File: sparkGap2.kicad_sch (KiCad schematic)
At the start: 44 parts, among them J1 9V, J2 IN, J3 OUT, Q1 BS170, SW2 pp, U1 TL072

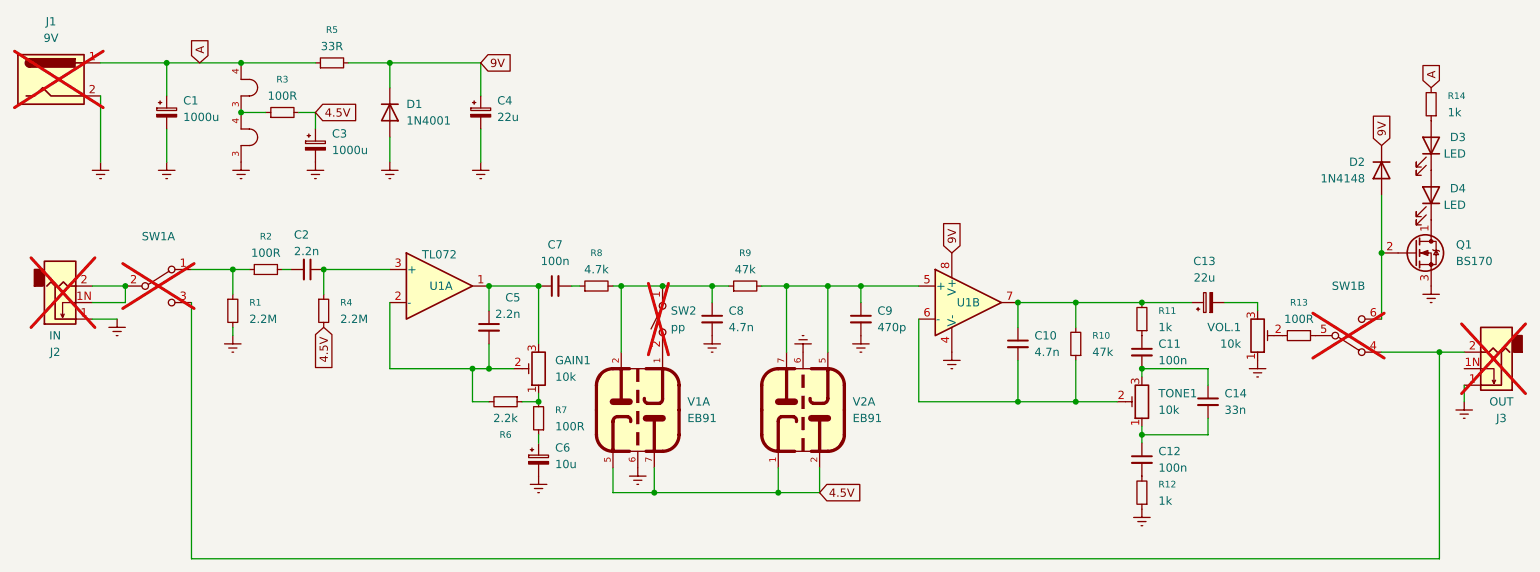
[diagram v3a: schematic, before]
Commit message: Slight adjustments to layout. Clean up component numbering.
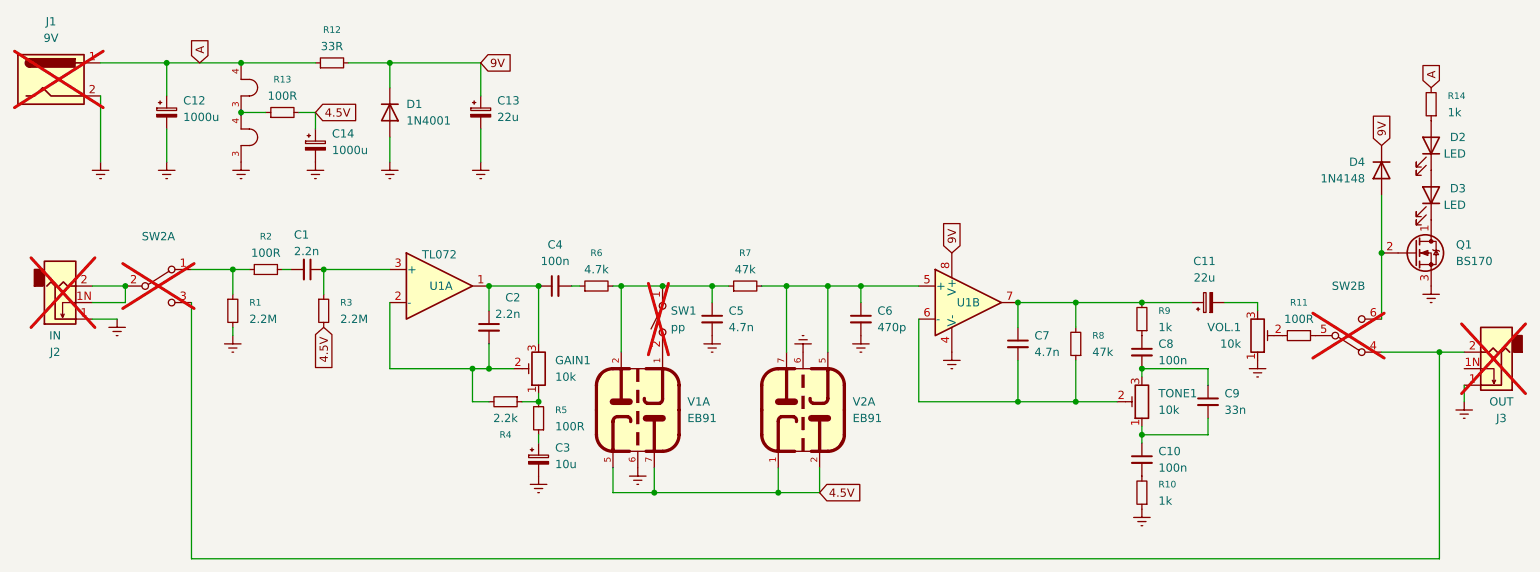
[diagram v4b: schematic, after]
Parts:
- renumbered C2 to C1, C12 to C10, C13 to C11, C1 to C12, C4 to C13, C3 to C14, C5 to C2, C6 to C3, C7 to C4, C8 to C5, C9 to C6, C10 to C7, C11 to C8, C14 to C9, D3 to D2, D4 to D3, D2 to D4, R12 to R10, R13 to R11, R5 to R12, R3 to R13, R4 to R3, R6 to R4, R7 to R5, R8 to R6, R9 to R7, R10 to R8, R11 to R9, SW2 to SW1, SW1 to SW2
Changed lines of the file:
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@@
 		(dnp no)
 		(fields_autoplaced yes)
-		(property "Reference" "R5"
+		(property "Reference" "R12"
 			(at 81.28 64.77 90)
 			(effects
@@
 			(project "sparkGap2"
 				(path "/bd6cf20e-4683-4745-aaa3-17469f6777ac"
-					(reference "R5")
+					(reference "R12")
 					(unit 1)
 				)
@@
 		(on_board yes)
 		(dnp no)
-		(property "Reference" "R6"
+		(property "Reference" "R4"
 			(at 107.95 127 90)
 			(effects
@@
 			(project "sparkGap2"
 				(path "/bd6cf20e-4683-4745-aaa3-17469f6777ac"
-					(reference "R6")
+					(reference "R4")
 					(unit 1)
 				)
@@
 		(on_board yes)
 		(dnp no)
-		(property "Reference" "C2"
+		(property "Reference" "C1"
 			(at 75.438 96.266 90)
 			(effects
@@
 			(project "sparkGap2"
 				(path "/bd6cf20e-4683-4745-aaa3-17469f6777ac"
-					(reference "C2")
+					(reference "C1")
 					(unit 1)
 				)
@@
 		(dnp no)
 		(fields_autoplaced yes)
-		(property "Reference" "C7"
+		(property "Reference" "C4"
 			(at 115.5763 97.79 90)
 			(effects
@@
 			(project "sparkGap2"
 				(path "/bd6cf20e-4683-4745-aaa3-17469f6777ac"
-					(reference "C7")
+					(reference "C4")
 					(unit 1)
 				)
@@
 		(dnp no)
 		(fields_autoplaced yes)
-		(property "Reference" "R4"
+		(property "Reference" "R3"
 			(at 82.55 106.6799 0)
 			(effects
@@
 			(project "sparkGap2"
 				(path "/bd6cf20e-4683-4745-aaa3-17469f6777ac"
-					(reference "R4")
+					(reference "R3")
 					(unit 1)
 				)
@@
 		(on_board yes)
 		(dnp no)
-		(property "Reference" "C5"
+		(property "Reference" "C2"
 			(at 110.236 105.918 0)
 			(effects
@@
 			(project "sparkGap2"
 				(path "/bd6cf20e-4683-4745-aaa3-17469f6777ac"
-					(reference "C5")
+					(reference "C2")
 					(unit 1)
 				)
@@
 		(dnp yes)
 		(fields_autoplaced yes)
-		(property "Reference" "SW1"
+		(property "Reference" "SW2"
 			(at 54.61 96.52 0)
 			(effects
@@
 			(project ""
 				(path "/bd6cf20e-4683-4745-aaa3-17469f6777ac"
-					(reference "SW1")
+					(reference "SW2")
 					(unit 1)
 				)
@@
 		(dnp no)
 		(fields_autoplaced yes)
-		(property "Reference" "C10"
+		(property "Reference" "C7"
 			(at 189.23 111.7662 0)
 			(effects
@@
 			(project "sparkGap2"
 				(path "/bd6cf20e-4683-4745-aaa3-17469f6777ac"
-					(reference "C10")
+					(reference "C7")
 					(unit 1)
 				)
@@
 		(dnp no)
 		(fields_autoplaced yes)
-		(property "Reference" "C12"
+		(property "Reference" "C10"
 			(at 208.28 129.5462 0)
 			(effects
@@
 			(project "sparkGap2"
 				(path "/bd6cf20e-4683-4745-aaa3-17469f6777ac"
-					(reference "C12")
+					(reference "C10")
 					(unit 1)
 				)
@@
 		(on_board yes)
 		(dnp no)
-		(property "Reference" "D3"
+		(property "Reference" "D2"
 			(at 255.524 81.28 90)
 			(effects
@@
 			(project "sparkGap2"
 				(path "/bd6cf20e-4683-4745-aaa3-17469f6777ac"
-					(reference "D3")
+					(reference "D2")
 					(unit 1)
 				)
@@
 		(dnp no)
 		(fields_autoplaced yes)
-		(property "Reference" "C11"
+		(property "Reference" "C8"
 			(at 208.28 113.0362 0)
 			(effects
@@
 			(project "sparkGap2"
 				(path "/bd6cf20e-4683-4745-aaa3-17469f6777ac"
-					(reference "C11")
+					(reference "C8")
 					(unit 1)
 				)
@@
 		(on_board yes)
 		(dnp no)
-		(property "Reference" "C4"
+		(property "Reference" "C13"
 			(at 106.68 75.6538 0)
 			(effects
@@
 			(project "sparkGap2"
 				(path "/bd6cf20e-4683-4745-aaa3-17469f6777ac"
-					(reference "C4")
+					(reference "C13")
 					(unit 1)
 				)
@@
 		(dnp no)
 		(fields_autoplaced yes)
-		(property "Reference" "C3"
+		(property "Reference" "C14"
 			(at 81.28 80.7338 0)
 			(effects
@@
 			(project "sparkGap2"
 				(path "/bd6cf20e-4683-4745-aaa3-17469f6777ac"
-					(reference "C3")
+					(reference "C14")
 					(unit 1)
 				)
@@
 		(dnp no)
 		(fields_autoplaced yes)
-		(property "Reference" "R10"
+		(property "Reference" "R8"
 			(at 198.12 111.7599 0)
 			(effects
@@
 			(project "sparkGap2"
 				(path "/bd6cf20e-4683-4745-aaa3-17469f6777ac"
-					(reference "R10")
+					(reference "R8")
 					(unit 1)
 				)
@@
 		(dnp yes)
 		(fields_autoplaced yes)
-		(property "Reference" "SW1"
+		(property "Reference" "SW2"
 			(at 237.49 104.14 0)
 			(effects
@@
 			(project ""
 				(path "/bd6cf20e-4683-4745-aaa3-17469f6777ac"
-					(reference "SW1")
+					(reference "SW2")
 					(unit 2)
 				)
@@
 		(on_board yes)
 		(dnp no)
-		(property "Reference" "D2"
+		(property "Reference" "D4"
 			(at 240.03 85.0899 90)
 			(effects
@@
 			(project "sparkGap2"
 				(path "/bd6cf20e-4683-4745-aaa3-17469f6777ac"
-					(reference "D2")
+					(reference "D4")
 					(unit 1)
 				)
@@
 		(dnp no)
 		(fields_autoplaced yes)
-		(property "Reference" "R12"
+		(property "Reference" "R10"
 			(at 208.28 134.6199 0)
 			(effects
@@
 			(project "sparkGap2"
 				(path "/bd6cf20e-4683-4745-aaa3-17469f6777ac"
-					(reference "R12")
+					(reference "R10")
 					(unit 1)
 				)
@@
 		(on_board yes)
 		(dnp no)
-		(property "Reference" "R9"
+		(property "Reference" "R7"
 			(at 144.78 99.06 90)
 			(effects
@@
 			(project "sparkGap2"
 				(path "/bd6cf20e-4683-4745-aaa3-17469f6777ac"
-					(reference "R9")
+					(reference "R7")
 					(unit 1)
 				)
@@
 		(dnp no)
 		(fields_autoplaced yes)
-		(property "Reference" "R7"
+		(property "Reference" "R5"
 			(at 115.57 123.1899 0)
 			(effects
@@
 			(project "sparkGap2"
 				(path "/bd6cf20e-4683-4745-aaa3-17469f6777ac"
-					(reference "R7")
+					(reference "R5")
 					(unit 1)
 				)
@@
 		(dnp no)
 		(fields_autoplaced yes)
-		(property "Reference" "C1"
+		(property "Reference" "C12"
 			(at 58.42 75.6538 0)
 			(effects
@@
 			(project "sparkGap2"
 				(path "/bd6cf20e-4683-4745-aaa3-17469f6777ac"
-					(reference "C1")
+					(reference "C12")
 					(unit 1)
 				)
@@
 		(dnp yes)
 		(fields_autoplaced yes)
-		(property "Reference" "SW2"
+		(property "Reference" "SW1"
 			(at 133.35 107.9499 90)
 			(effects
@@
 			(project ""
 				(path "/bd6cf20e-4683-4745-aaa3-17469f6777ac"
-					(reference "SW2")
+					(reference "SW1")
 					(unit 1)
 				)
@@
 		(dnp no)
 		(fields_autoplaced yes)
-		(property "Reference" "C13"
+		(property "Reference" "C11"
 			(at 215.3539 100.33 90)
 			(effects
@@
 			(project "sparkGap2"
 				(path "/bd6cf20e-4683-4745-aaa3-17469f6777ac"
-					(reference "C13")
+					(reference "C11")
 					(unit 1)
 				)
@@
 		(dnp no)
 		(fields_autoplaced yes)
-		(property "Reference" "R13"
+		(property "Reference" "R11"
 			(at 229.87 106.68 90)
 			(effects
@@
 			(project "sparkGap2"
 				(path "/bd6cf20e-4683-4745-aaa3-17469f6777ac"
-					(reference "R13")
+					(reference "R11")
 					(unit 1)
 				)
@@
 		(dnp no)
 		(fields_autoplaced yes)
-		(property "Reference" "C8"
+		(property "Reference" "C5"
 			(at 142.24 107.9562 0)
 			(effects
@@
 			(project "sparkGap2"
 				(path "/bd6cf20e-4683-4745-aaa3-17469f6777ac"
-					(reference "C8")
+					(reference "C5")
 					(unit 1)
 				)
@@
 		(dnp no)
 		(fields_autoplaced yes)
-		(property "Reference" "C6"
+		(property "Reference" "C3"
 			(at 115.57 128.9938 0)
 			(effects
@@
 			(project ""
 				(path "/bd6cf20e-4683-4745-aaa3-17469f6777ac"
-					(reference "C6")
+					(reference "C3")
 					(unit 1)
 				)
@@
 		(dnp no)
 		(fields_autoplaced yes)
-		(property "Reference" "R11"
+		(property "Reference" "R9"
 			(at 208.28 107.9499 0)
 			(effects
@@
 			(project "sparkGap2"
 				(path "/bd6cf20e-4683-4745-aaa3-17469f6777ac"
-					(reference "R11")
+					(reference "R9")
 					(unit 1)
 				)
@@
 		(dnp no)
 		(fields_autoplaced yes)
-		(property "Reference" "C9"
+		(property "Reference" "C6"
 			(at 165.1 107.9562 0)
 			(effects
@@
 			(project "sparkGap2"
 				(path "/bd6cf20e-4683-4745-aaa3-17469f6777ac"
-					(reference "C9")
+					(reference "C6")
 					(unit 1)
 				)
@@
 		(dnp no)
 		(fields_autoplaced yes)
-		(property "Reference" "R3"
+		(property "Reference" "R13"
 			(at 73.66 72.39 90)
 			(effects
@@
 			(project "sparkGap2"
 				(path "/bd6cf20e-4683-4745-aaa3-17469f6777ac"
-					(reference "R3")
+					(reference "R13")
 					(unit 1)
 				)
@@
 		(on_board yes)
 		(dnp no)
-		(property "Reference" "D4"
+		(property "Reference" "D3"
 			(at 255.524 89.154 90)
 			(effects
@@
 			(project "sparkGap2"
 				(path "/bd6cf20e-4683-4745-aaa3-17469f6777ac"
-					(reference "D4")
+					(reference "D3")
 					(unit 1)
 				)
@@
 		(on_board yes)
 		(dnp no)
-		(property "Reference" "R8"
+		(property "Reference" "R6"
 			(at 121.92 99.06 90)
 			(effects
@@
 			(project "sparkGap2"
 				(path "/bd6cf20e-4683-4745-aaa3-17469f6777ac"
-					(reference "R8")
+					(reference "R6")
 					(unit 1)
 				)
@@
 		(dnp no)
 		(fields_autoplaced yes)
-		(property "Reference" "C14"
+		(property "Reference" "C9"
 			(at 218.44 120.6562 0)
 			(effects
@@
 			(project "sparkGap2"
 				(path "/bd6cf20e-4683-4745-aaa3-17469f6777ac"
-					(reference "C14")
+					(reference "C9")
 					(unit 1)
 				)

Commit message: Address issues found with last production run
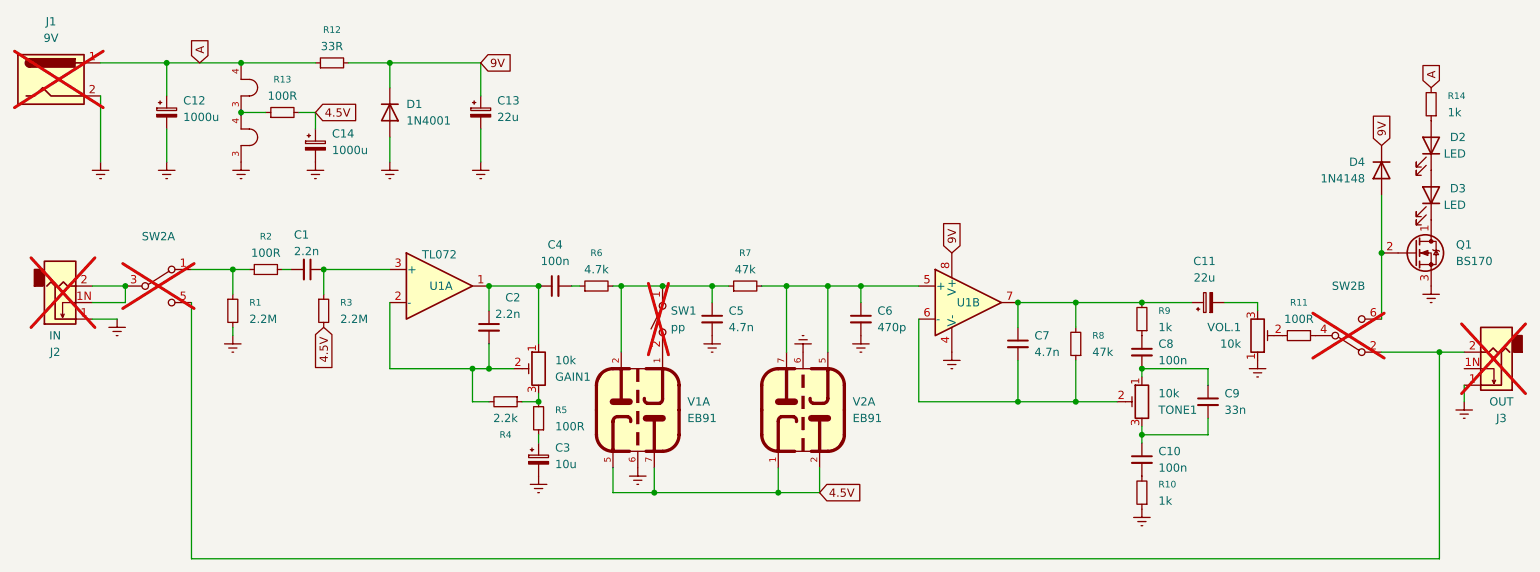
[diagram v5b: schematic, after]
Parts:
- SW2: footprint Connector_PinSocket_2.54mm:PinSocket_2x03_P2.54mm_Vertical -> SamacSys_Parts:DPDT
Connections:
- net at J2.1N, J2.2: now also SW2.3; no longer SW2.2
- net at R4.1, R5.2: now also GAIN1.3; no longer GAIN1.1
- net at C2.1, C4.1, U1.1: now also GAIN1.1; no longer GAIN1.3
- net at C10.1, C9.2: now also TONE1.3; no longer TONE1.1
- net at C8.2, C9.1: now also TONE1.1; no longer TONE1.3
- net at R11.1: now also SW2.4; no longer SW2.5
- new net: J3.2, SW2.2, SW2.5
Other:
- moved on the sheet: GAIN1, TONE1
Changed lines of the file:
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@@
 			)
 		)
-		(property "Footprint" "Connector_PinSocket_2.54mm:PinSocket_2x03_P2.54mm_Vertical"
+		(property "Footprint" "SamacSys_Parts:DPDT"
 			(at 55.88 104.14 0)
 			(effects
@@
 			)
 		)
-		(property "Footprint" "Connector_PinSocket_2.54mm:PinSocket_2x03_P2.54mm_Vertical"
+		(property "Footprint" "SamacSys_Parts:DPDT"
 			(at 238.76 111.76 0)
 			(effects
@@
 	(symbol
 		(lib_id "Device:R_Potentiometer_Trim")
-		(at 205.74 121.92 180)
-		(unit 1)
-		(exclude_from_sim no)
-		(in_bom yes)
-		(on_board yes)
-		(dnp no)
-		(fields_autoplaced yes)
+		(at 205.74 121.92 0)
+		(mirror y)
+		(unit 1)
+		(exclude_from_sim no)
+		(in_bom yes)
+		(on_board yes)
+		(dnp no)
 		(property "Reference" "TONE1"
-			(at 208.28 120.6499 0)
+			(at 208.28 123.1901 0)
 			(effects
 				(font
@@
 		)
 		(property "Value" "10k"
-			(at 208.28 123.1899 0)
+			(at 208.28 120.6501 0)
 			(effects
 				(font
@@
 	(symbol
 		(lib_id "Device:R_Potentiometer_Trim")
-		(at 113.03 116.84 180)
-		(unit 1)
-		(exclude_from_sim no)
-		(in_bom yes)
-		(on_board yes)
-		(dnp no)
-		(fields_autoplaced yes)
+		(at 113.03 116.84 0)
+		(mirror y)
+		(unit 1)
+		(exclude_from_sim no)
+		(in_bom yes)
+		(on_board yes)
+		(dnp no)
 		(property "Reference" "GAIN1"
-			(at 115.57 115.5699 0)
+			(at 115.57 118.1101 0)
 			(effects
 				(font
@@
 		)
 		(property "Value" "10k"
-			(at 115.57 118.1099 0)
+			(at 115.57 115.5701 0)
 			(effects
 				(font
@@
 		)
 		(instances
-			(project ""
+			(project "sparkGap2"
 				(path "/bd6cf20e-4683-4745-aaa3-17469f6777ac"
 					(reference "GAIN1")

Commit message: add build guide, improve BOM, gen production
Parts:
- J1, J2, J3: now left out of the parts list
- SW1: value pp -> SPST
- SW2: value ~ -> 6-pin Footswitch
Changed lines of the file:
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@@
 		(unit 1)
 		(exclude_from_sim no)
-		(in_bom yes)
+		(in_bom no)
 		(on_board yes)
 		(dnp yes)
@@
 		(unit 1)
 		(exclude_from_sim no)
-		(in_bom yes)
+		(in_bom no)
 		(on_board yes)
 		(dnp yes)
@@
 			)
 		)
-		(property "Value" "~"
+		(property "Value" "6-pin Footswitch"
 			(at 54.61 99.06 0)
 			(effects
@@
 					(size 1.27 1.27)
 				)
+				(hide yes)
 			)
 		)
@@
 			)
 		)
-		(property "Value" "~"
+		(property "Value" "6-pin Footswitch"
 			(at 237.49 106.68 0)
 			(effects
@@
 					(size 1.27 1.27)
 				)
+				(hide yes)
 			)
 		)
@@
 		(fields_autoplaced yes)
 		(property "Reference" "SW1"
-			(at 133.35 107.9499 90)
+			(at 133.35 109.2199 90)
 			(effects
 				(font
@@
 			)
 		)
-		(property "Value" "pp"
+		(property "Value" "SPST"
 			(at 133.35 110.4899 90)
 			(effects
@@
 				)
 				(justify right)
+				(hide yes)
 			)
 		)
@@
 		(unit 1)
 		(exclude_from_sim no)
-		(in_bom yes)
+		(in_bom no)
 		(on_board yes)
 		(dnp yes)

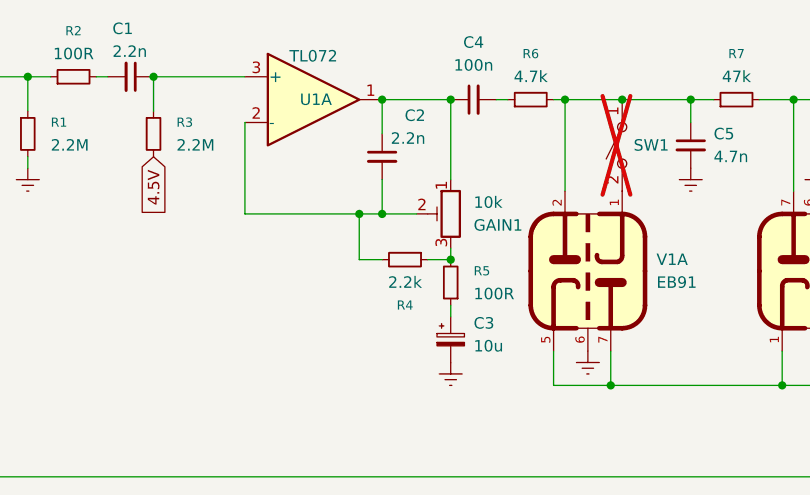
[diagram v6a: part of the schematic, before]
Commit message: Update SVG, CNC files. Improve traces around pots
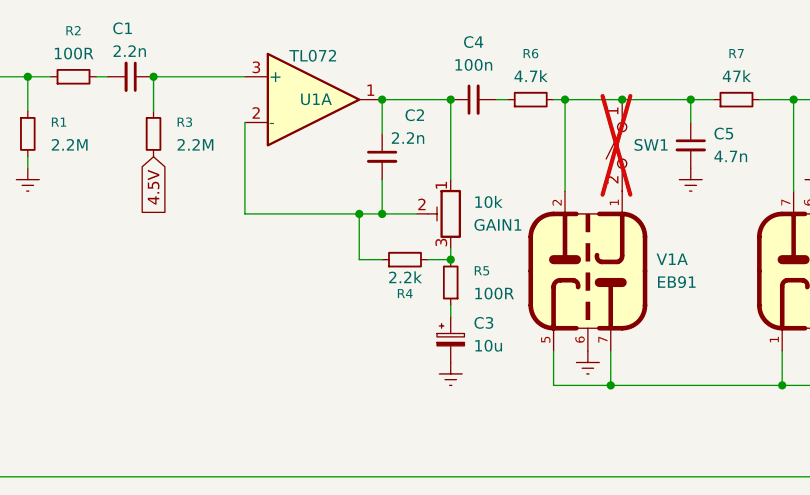
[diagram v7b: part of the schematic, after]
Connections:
- net at GAIN1.3, R5.2: now also R4.2; no longer R4.1
- net at C2.2, GAIN1.2, U1.2 (-): now also R4.1; no longer R4.2
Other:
- moved on the sheet: R4
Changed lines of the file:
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@@
 	(symbol
 		(lib_id "Device:R_Small")
-		(at 107.95 121.92 270)
+		(at 107.95 121.92 90)
 		(unit 1)
 		(exclude_from_sim no)
@@
 		(dnp no)
 		(property "Reference" "R4"
-			(at 107.95 127 90)
+			(at 107.95 125.73 90)
 			(effects
 				(font
@@
 		)
 		(property "Value" "2.2k"
-			(at 107.95 124.46 90)
+			(at 107.95 123.952 90)
 			(effects
 				(font
